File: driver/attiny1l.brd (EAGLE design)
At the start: 35.8 x 20 mm, 7 parts, among them IC1 ATTiny85, IC2 74AHC1G00DCK, IC3 74AHC1G00DCK, IC4 LB1973M, J1 AVR_SPI_PRG_6NS

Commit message: very quick and dirty reorg for new footprint
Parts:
- moved IC3 2.10 mm to (22.2, 5.46), turned to 270 degrees
- moved IC2 1.45 mm to (23.0, 14.9), turned to 270 degrees
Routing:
- net IN2: track 5.03 -> 13.1 mm
- net IN1/MISO: track 69.8 -> 72.7 mm
- net IN3: track 15.4 -> 14.0 mm
- net IN4: track 6.15 -> 7.16 mm
- net +5V: track 46.8 -> 46.3 mm

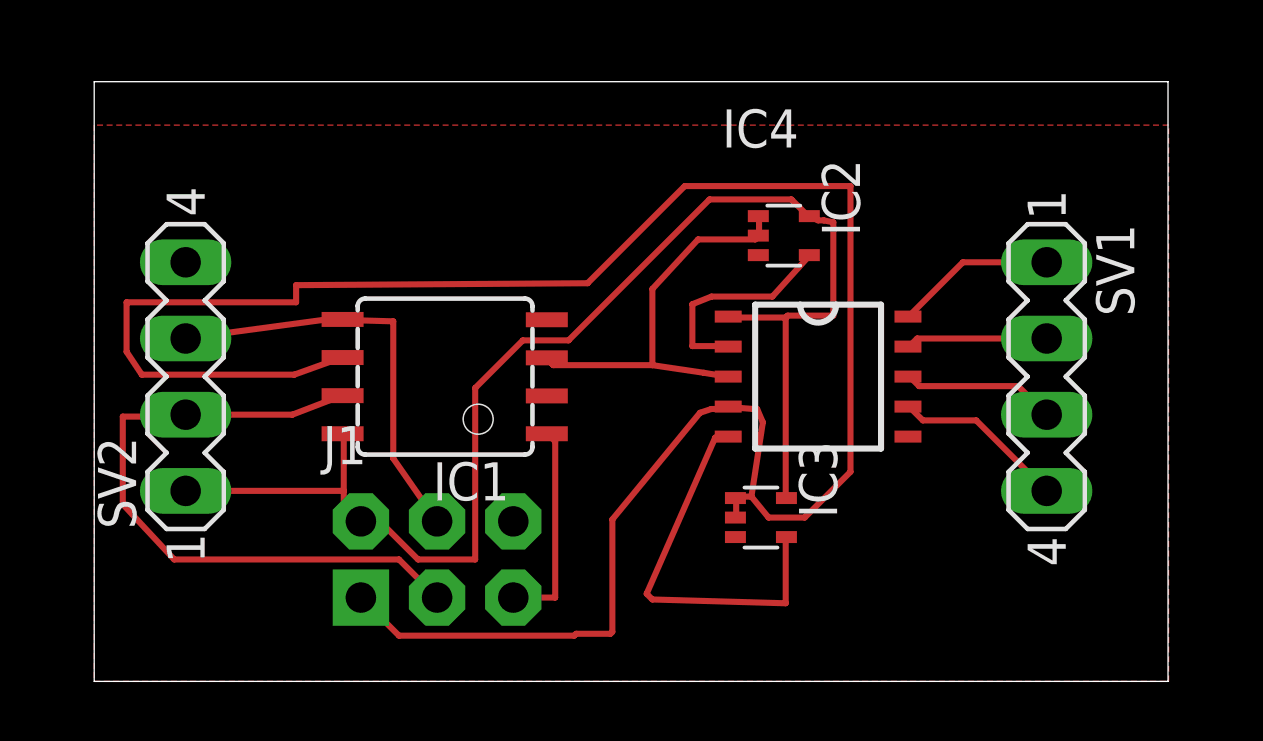
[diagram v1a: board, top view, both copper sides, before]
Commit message: use dual NOT and added bypass caps
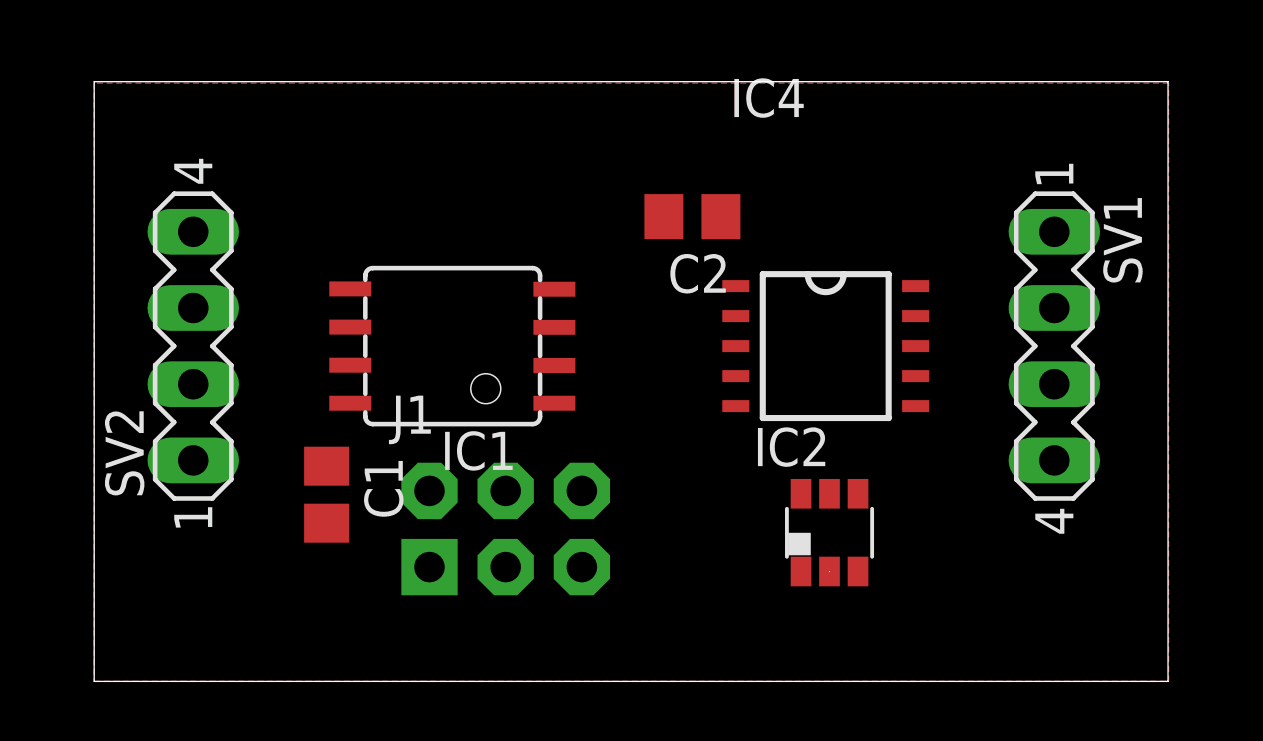
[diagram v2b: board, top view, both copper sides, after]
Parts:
- removed IC3: 74AHC1G00DCK, 74xx-little-de:SC70-5
- added C1, C2: (no value), rcl:C0805
- IC2: value 74AHC1G00DCK -> (none); device 74xx-little-de:SC70-5 -> dp_devices:DBV-R-PDSO-G6
- moved IC2 10.0 mm to (24.5, 4.95), turned to 0 degrees
- moved J1 2.50 mm to (13.7, 5.08)
- moved IC1 1.05 mm to (11.9, 11.2)
- moved IC4 1.05 mm to (24.4, 11.2)
- moved SV2 1.05 mm to (3.30, 11.2)
- moved SV1 1.05 mm to (32.0, 11.2)
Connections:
- removed net IN3: IC1.3, IC2.1, IC2.2, IC4.3
- removed net IN4: IC2.4, IC4.2
- new net N$1: IC1.3, IC2.1, IC4.3
- new net N$2: IC2.6, IC4.2
- net +5V: now also C1.1, C2.1; no longer IC3.5
- net GND: now also C1.2, C2.2, IC2.2; no longer IC2.3, IC3.3
- net IN1/MISO: now also IC2.3; no longer IC3.1, IC3.2
- net IN2: now also IC2.4; no longer IC3.4
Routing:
- net IN1/MISO: track 72.7 -> 0.00 mm
- net +5V: track 46.3 -> 0.00 mm
- net SCL/SCK: track 22.2 -> 0.00 mm
- net SDA/MOSI: track 14.6 -> 0.00 mm
- net IN3: track 14.0 -> 0.00 mm
- net IN2: track 13.1 -> 0.00 mm
- net IN4: track 7.16 -> 0.00 mm
- net N$6: track 6.99 -> 0.00 mm
- net OUT2: track 5.78 -> 0.00 mm
- net OUT4: track 5.37 -> 0.00 mm
- net OUT1: track 5.15 -> 0.00 mm
- net OUT3: track 4.73 -> 0.00 mm

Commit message: QnD routed
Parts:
- moved IC2 8.45 mm to (18.8, 11.2), turned to 270 degrees
- moved C2 3.69 mm to (23.6, 15.4), turned to 90 degrees
- moved IC4 2.92 mm to (27.3, 11.0)
- moved IC1 1.92 mm to (10.0, 11.4)
- moved C1 1.40 mm to (6.35, 6.22)
- moved SV1 1.27 mm to (33.3, 11.2)
- moved J1 1.15 mm to (12.6, 4.95)
- moved SV2 0.89 mm to (2.41, 11.2)
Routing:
- net +5V: track 0.00 -> 57.7 mm
- net IN1/MISO: track 0.00 -> 50.9 mm
- net N$1: track 0.00 -> 25.1 mm
- net SDA/MOSI: track 0.00 -> 16.6 mm
- net SCL/SCK: track 0.00 -> 14.7 mm
- net N$6: track 0.00 -> 7.29 mm
- net IN2: track 0.00 -> 4.84 mm
- net N$2: track 0.00 -> 4.28 mm
- net OUT2: track 0.00 -> 4.23 mm
- net OUT4: track 0.00 -> 3.77 mm
- net OUT1: track 0.00 -> 3.45 mm
- net OUT3: track 0.00 -> 3.13 mm

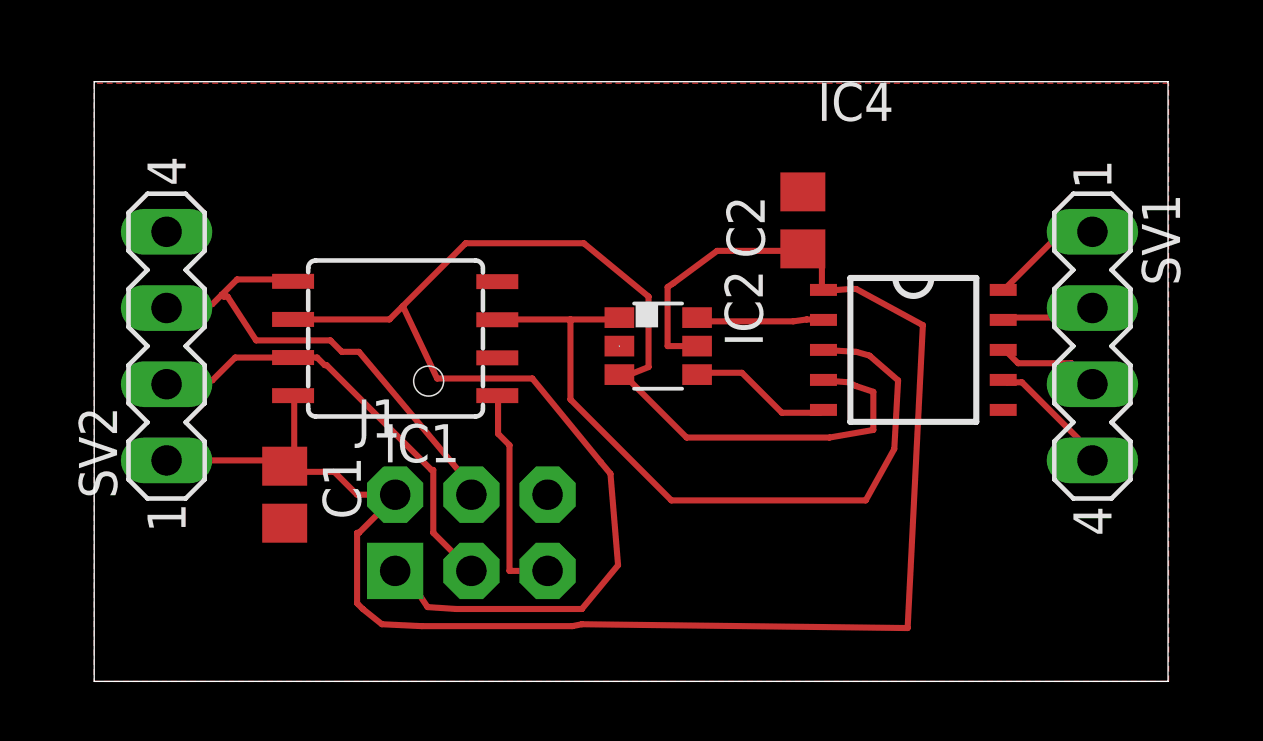
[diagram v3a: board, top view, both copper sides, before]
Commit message: added some more jumper to hopefully get better ground connections
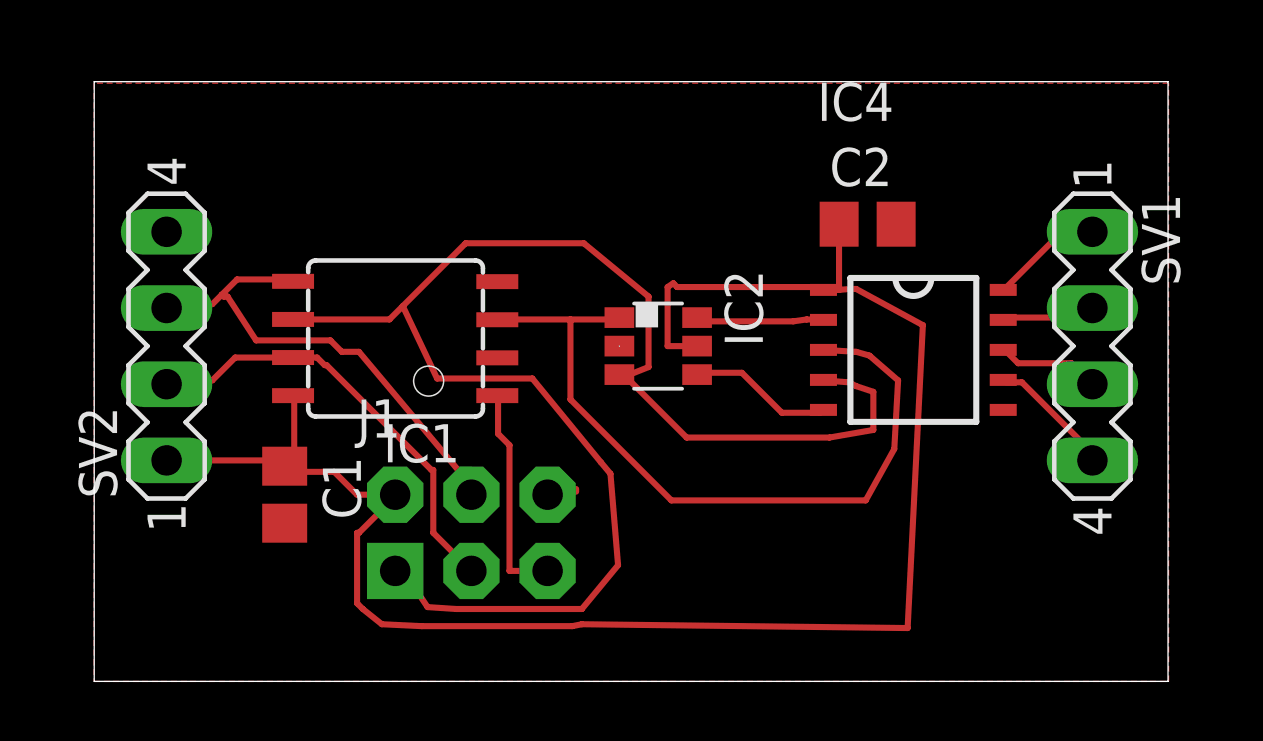
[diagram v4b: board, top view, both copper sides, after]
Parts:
- moved C2 2.16 mm to (25.8, 15.2), turned to 0 degrees
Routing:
- net GND: track 0.00 -> 0.78 mm
- net +5V: track 57.7 -> 58.3 mm
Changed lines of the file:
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@@
 <element name="IC2" library="dp_devices" package="DBV-R-PDSO-G6" value="" x="18.796" y="11.176" rot="R270"/>
 <element name="C1" library="rcl" package="C0805" value="" x="6.35" y="6.223" rot="R270"/>
-<element name="C2" library="rcl" package="C0805" value="" x="23.622" y="15.367" rot="R90"/>
+<element name="C2" library="rcl" package="C0805" value="" x="25.781" y="15.24"/>
 </elements>
 <signals>
@@
 <contactref element="C1" pad="2"/>
 <contactref element="C2" pad="2"/>
-<wire x1="17.506" y1="11.176" x2="23.622" y2="16.317" width="0" layer="19" extent="1-1"/>
+<wire x1="15.6845" y1="6.4135" x2="15.6845" y2="6.32459375" width="0.2032" layer="1"/>
+<wire x1="15.6845" y1="6.4135" x2="15.113" y2="6.223" width="0.2032" layer="1"/>
+<wire x1="16.0655" y1="6.4135" x2="16.0655" y2="6.32459375" width="0.2032" layer="1"/>
+<wire x1="17.506" y1="11.176" x2="16.0655" y2="6.4135" width="0" layer="19" extent="1-1"/>
 <wire x1="13.437" y1="13.325" x2="17.506" y2="11.176" width="0" layer="19" extent="1-1"/>
-<wire x1="15.113" y1="6.223" x2="17.506" y2="11.176" width="0" layer="19" extent="1-1"/>
+<wire x1="6.35" y1="5.273" x2="15.113" y2="6.223" width="0" layer="19" extent="1-1"/>
 </signal>
 <signal name="+5V">
@@
 <contactref element="C1" pad="1"/>
 <contactref element="C2" pad="1"/>
-<wire x1="24.257" y1="14.4145" x2="24.257" y2="13.081" width="0.2032" layer="1"/>
-<wire x1="23.622" y1="14.4145" x2="24.257" y2="14.4145" width="0.2032" layer="1"/>
 <wire x1="24.257" y1="13.081" x2="24.309" y2="13.049" width="0.2032" layer="1"/>
-<wire x1="23.622" y1="14.4145" x2="23.622" y2="14.417" width="0.2032" layer="1"/>
 <wire x1="19.1135" y1="11.176" x2="20.096" y2="11.176" width="0.2032" layer="1"/>
 <wire x1="19.1135" y1="13.1445" x2="19.1135" y2="11.176" width="0.2032" layer="1"/>
 <wire x1="19.304" y1="13.2715" x2="19.1135" y2="13.1445" width="0.2032" layer="1"/>
-<wire x1="20.7645" y1="14.351" x2="19.304" y2="13.2715" width="0.2032" layer="1"/>
-<wire x1="23.5585" y1="14.351" x2="20.7645" y2="14.351" width="0.2032" layer="1"/>
-<wire x1="23.5585" y1="14.351" x2="23.622" y2="14.417" width="0.2032" layer="1"/>
 <wire x1="6.6675" y1="7.1755" x2="6.6675" y2="9.525" width="0.2032" layer="1"/>
 <wire x1="6.35" y1="7.1755" x2="6.6675" y2="7.1755" width="0.2032" layer="1"/>
@@
 <wire x1="6.604" y1="7.366" x2="2.413" y2="7.366" width="0.2032" layer="1"/>
 <wire x1="6.604" y1="7.366" x2="6.35" y2="7.173" width="0.2032" layer="1"/>
-<wire x1="25.2095" y1="13.081" x2="24.384" y2="13.0175" width="0.2032" layer="1"/>
+<wire x1="25.2095" y1="13.081" x2="24.835596875" y2="13.0522375" width="0.2032" layer="1"/>
+<wire x1="24.835596875" y1="13.0522375" x2="24.384" y2="13.0175" width="0.2032" layer="1"/>
 <wire x1="25.4" y1="13.081" x2="25.2095" y2="13.081" width="0.2032" layer="1"/>
 <wire x1="27.6225" y1="11.8745" x2="25.4" y2="13.081" width="0.2032" layer="1"/>
@@
 <wire x1="24.384" y1="13.0175" x2="24.309" y2="13.049" width="0.2032" layer="1"/>
 <wire x1="10.033" y1="6.1595" x2="10.033" y2="6.223" width="0.2032" layer="1"/>
+<wire x1="24.8285" y1="13.1445" x2="24.8285" y2="15.24" width="0.2032" layer="1"/>
+<wire x1="24.8285" y1="15.24" x2="24.831" y2="15.24" width="0.2032" layer="1"/>
+<wire x1="24.8285" y1="13.1445" x2="24.835596875" y2="13.0522375" width="0.2032" layer="1"/>
+<wire x1="24.1935" y1="13.1445" x2="19.431" y2="13.1445" width="0.2032" layer="1"/>
+<wire x1="19.431" y1="13.1445" x2="19.304" y2="13.2715" width="0.2032" layer="1"/>
+<wire x1="24.1935" y1="13.1445" x2="24.309" y2="13.049" width="0.2032" layer="1"/>
 </signal>
 <signal name="SDA/MOSI">

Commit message: added a debugging led
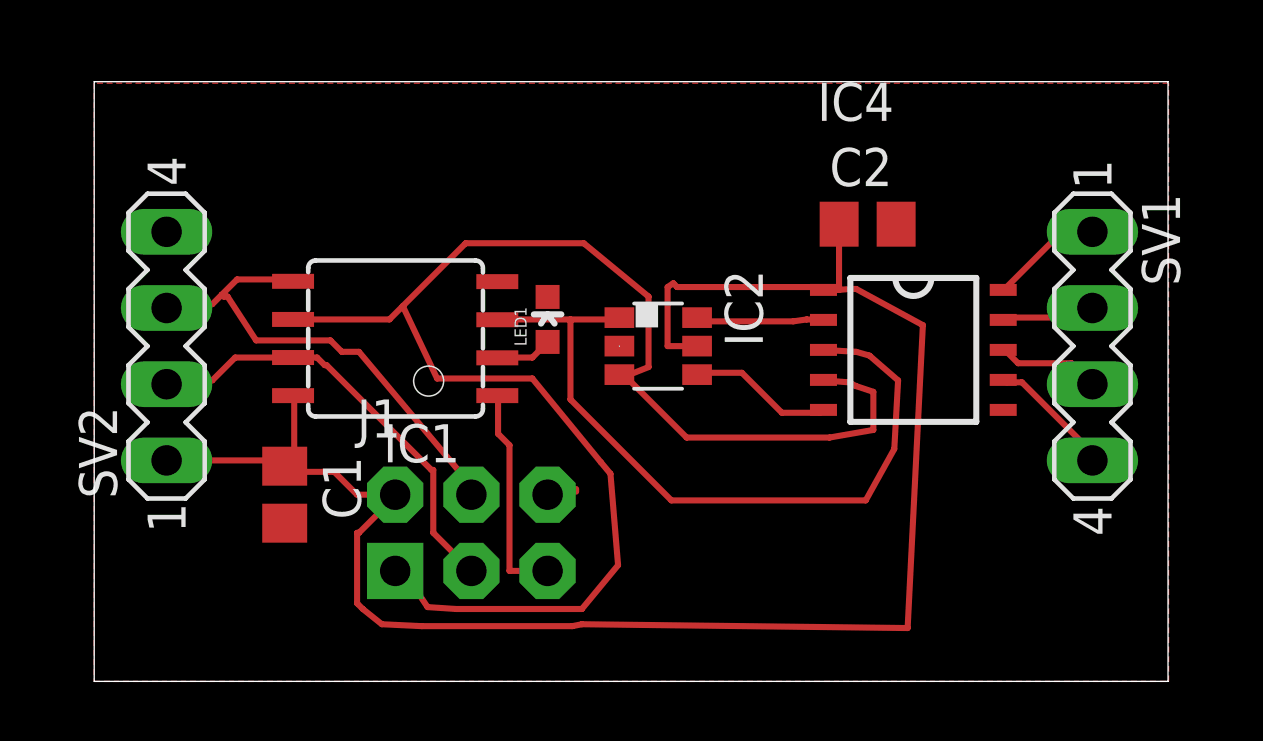
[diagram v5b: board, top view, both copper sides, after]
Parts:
- added LED1: (no value), SparkFun-LED:LED-0603
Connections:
- new net N$3: IC1.2, LED1.A
- net GND: now also LED1.C
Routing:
- net N$3: track 0.00 -> 1.90 mm
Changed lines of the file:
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@@
 <element name="C1" library="rcl" package="C0805" value="" x="6.35" y="6.223" rot="R270"/>
 <element name="C2" library="rcl" package="C0805" value="" x="25.781" y="15.24"/>
+<element name="LED1" library="SparkFun-LED" package="LED-0603" value="" x="15.113" y="12.065"/>
 </elements>
 <signals>
@@
 <wire x1="15.6845" y1="6.4135" x2="15.113" y2="6.223" width="0.2032" layer="1"/>
 <wire x1="16.0655" y1="6.4135" x2="16.0655" y2="6.32459375" width="0.2032" layer="1"/>
+<contactref element="LED1" pad="C"/>
+<wire x1="30.353" y1="9.0805" x2="30.301" y2="9.049" width="0.2032" layer="1"/>
+<wire x1="30.353" y1="9.0805" x2="30.30103125" y2="9.0490125" width="0.2032" layer="1"/>
+<wire x1="30.2895" y1="9.0805" x2="30.301" y2="9.049" width="0.2032" layer="1"/>
+<wire x1="30.2895" y1="9.0805" x2="30.30103125" y2="9.0490125" width="0.2032" layer="1"/>
 <wire x1="17.506" y1="11.176" x2="16.0655" y2="6.4135" width="0" layer="19" extent="1-1"/>
-<wire x1="13.437" y1="13.325" x2="17.506" y2="11.176" width="0" layer="19" extent="1-1"/>
+<wire x1="15.113" y1="12.815" x2="17.506" y2="11.176" width="0" layer="19" extent="1-1"/>
 <wire x1="6.35" y1="5.273" x2="15.113" y2="6.223" width="0" layer="19" extent="1-1"/>
 </signal>
@@
 <wire x1="20.1295" y1="12.065" x2="20.096" y2="12.126" width="0.2032" layer="1"/>
 </signal>
+<signal name="N$3">
+<contactref element="IC1" pad="2"/>
+<contactref element="LED1" pad="A"/>
+<wire x1="14.605" y1="10.795" x2="15.113" y2="11.303" width="0.2032" layer="1"/>
+<wire x1="13.462" y1="10.795" x2="14.605" y2="10.795" width="0.2032" layer="1"/>
+<wire x1="15.113" y1="11.303" x2="15.113" y2="11.315" width="0.2032" layer="1"/>
+<wire x1="13.462" y1="10.795" x2="13.437" y2="10.785" width="0.2032" layer="1"/>
+</signal>
 </signals>
